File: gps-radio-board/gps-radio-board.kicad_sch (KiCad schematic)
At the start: 61 parts, among them J1 SMA, J2 SMA, J3 USB_C_Receptacle_USB2.0_16P, J4 JST_BATT, J5 Conn_01x04, J6 Conn_01x04, J7 Conn_01x04, J8 DM3CS-SF, U1 ESP32-C6-MINI-1U-H4, U3 SiP32431DR3, U4 AP2112K-3.3, U5 MAX-M10N, U6 MCP73831, U7 AP2112K-3.3

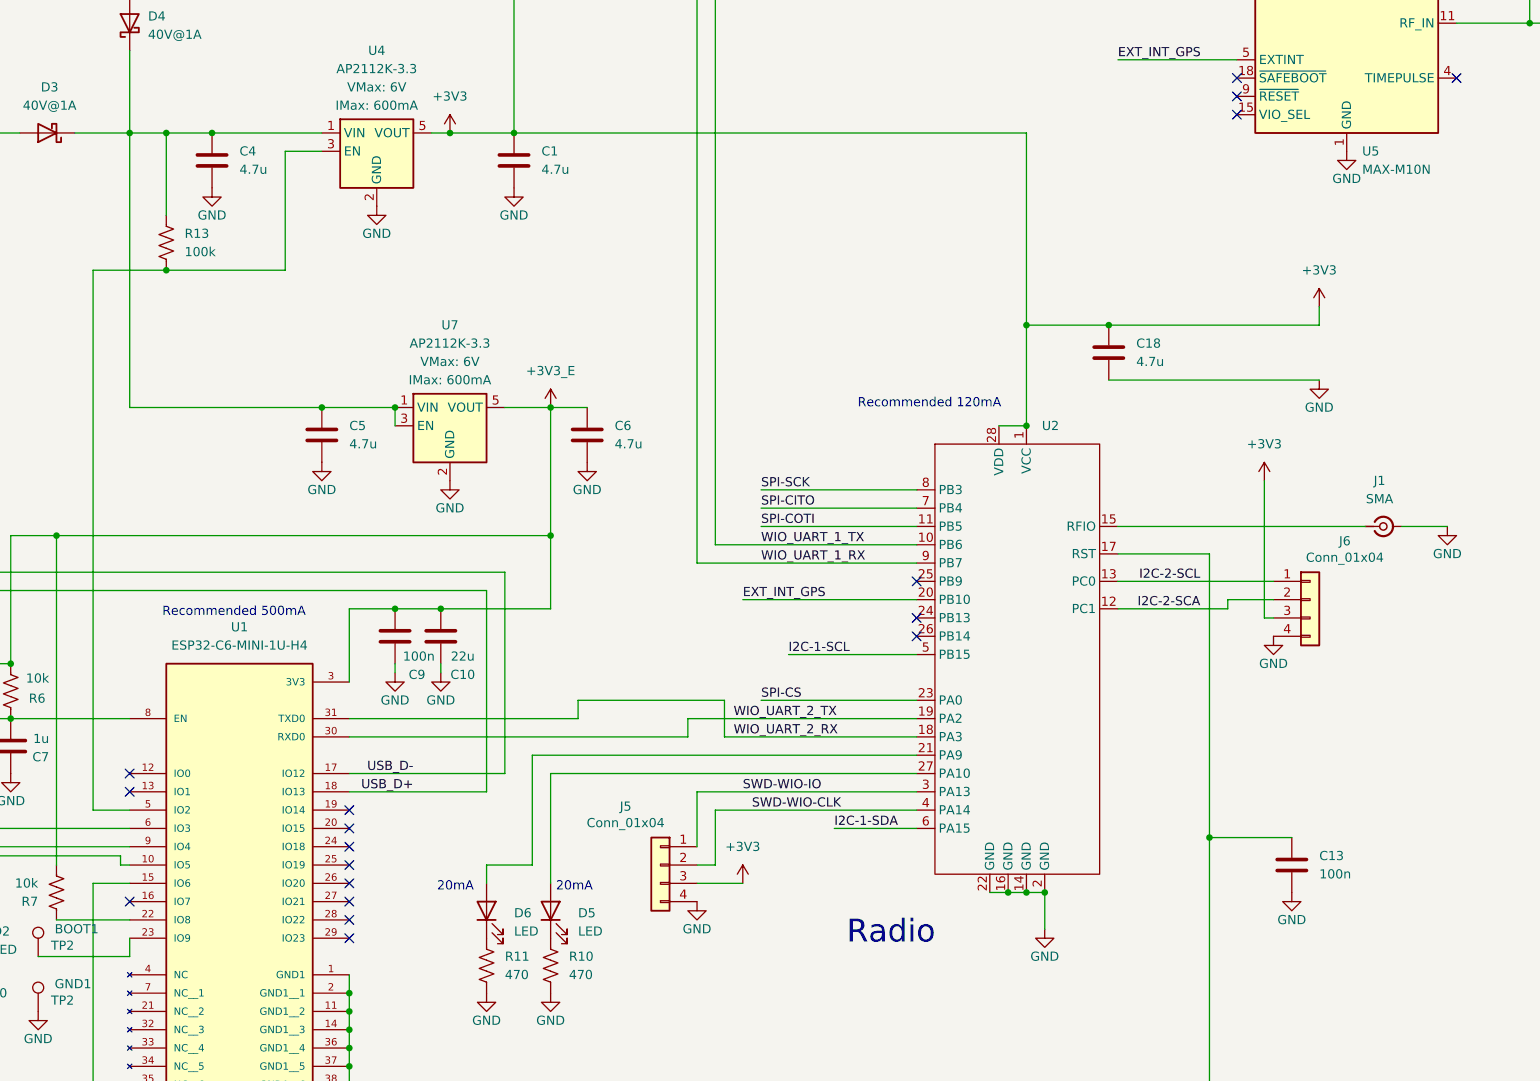
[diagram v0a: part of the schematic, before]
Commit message: Layout fixes. Swap 100k ref for en
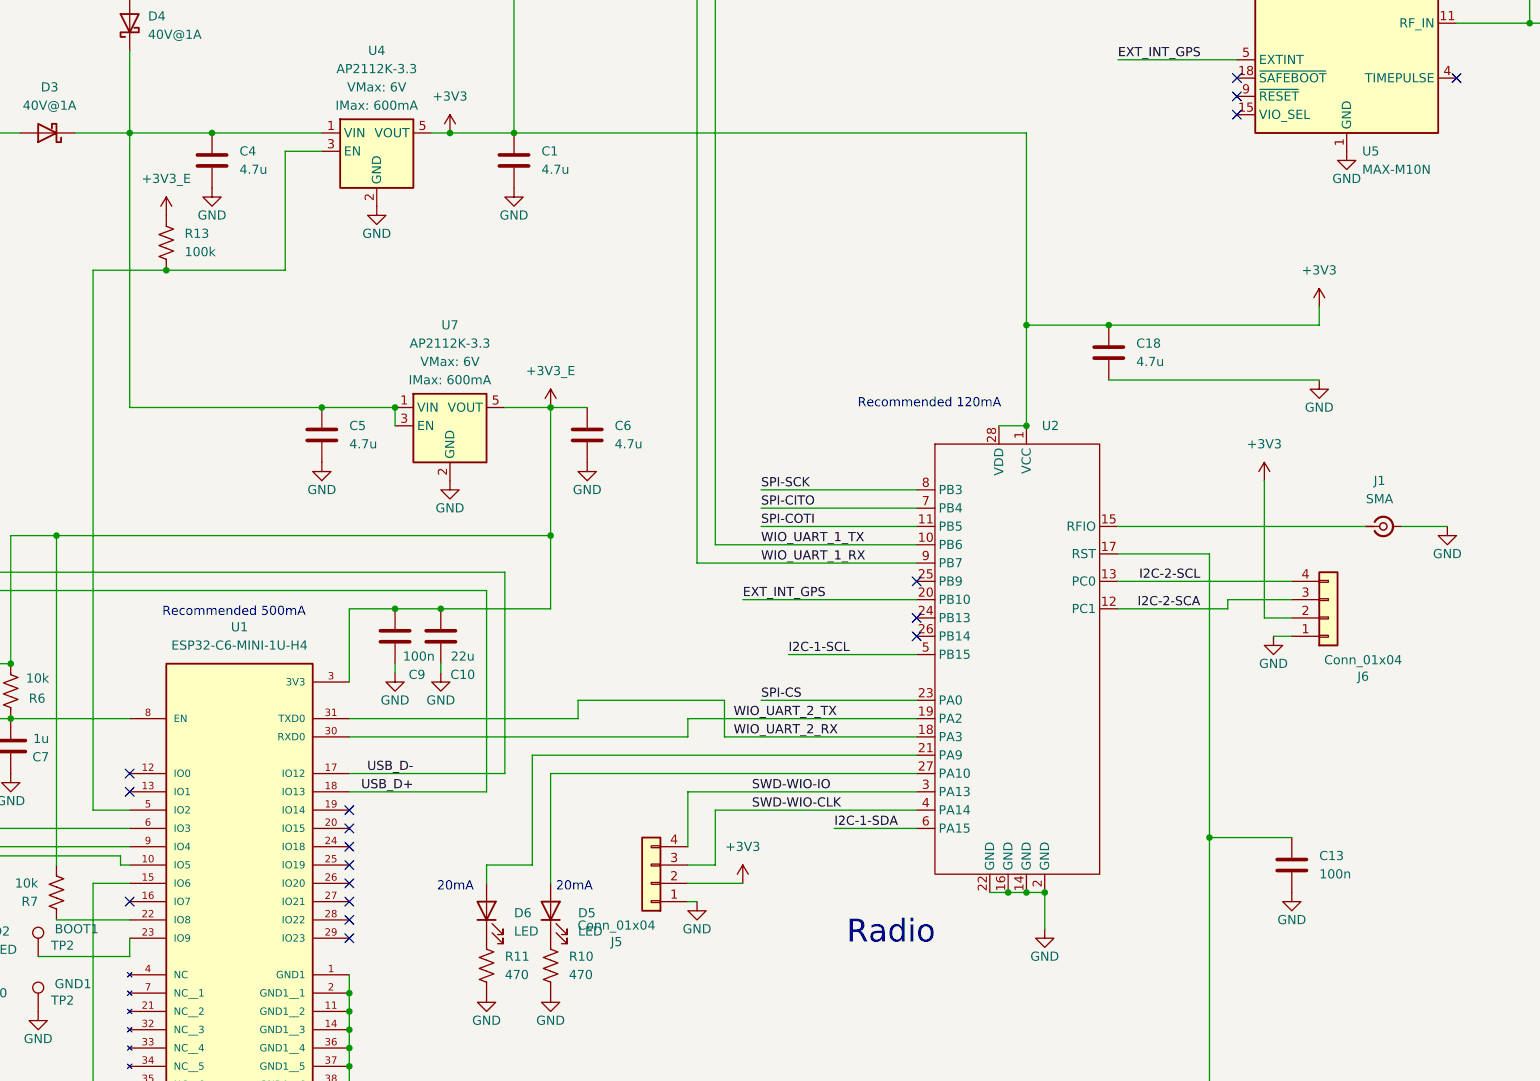
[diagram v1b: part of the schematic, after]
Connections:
- net +3V3: now also J5.2 (Pin_2), J6.2 (Pin_2); no longer J5.3 (Pin_3), J6.3 (Pin_3)
- net +3V3_E: now also R13.2
- net GND: now also J5.1 (Pin_1), J6.1 (Pin_1); no longer J5.4 (Pin_4), J6.4 (Pin_4)
- net I2C-2-SCA: now also J6.3 (Pin_3); no longer J6.2 (Pin_2)
- net I2C-2-SCL: now also J6.4 (Pin_4); no longer J6.1 (Pin_1)
- net SWD-WIO-CLK: now also J5.3 (Pin_3); no longer J5.2 (Pin_2)
- net SWD-WIO-IO: now also J5.4 (Pin_4); no longer J5.1 (Pin_1)
- net at C4.1, C5.1, D3.1 (K)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: no longer R13.2
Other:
- moved on the sheet: J5, J6
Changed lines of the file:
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@@
 	)
 	(junction
-		(at 224.79 132.08)
-		(diameter 0)
-		(color 0 0 0 0)
-	)
-	(junction
 		(at 250.19 287.02)
 		(diameter 0)
@@
 	(wire
 		(pts
+			(xy 356.87 194.31) (xy 381 194.31)
+		)
+		(stroke
+			(width 0)
+			(type default)
+		)
+	)
+	(wire
+		(pts
 			(xy 241.3 134.62) (xy 241.3 151.13)
 		)
@@
 	(wire
 		(pts
+			(xy 297.18 238.76) (xy 298.45 238.76)
+		)
+		(stroke
+			(width 0)
+			(type default)
+		)
+	)
+	(wire
+		(pts
 			(xy 189.23 232.41) (xy 189.23 237.49)
 		)
@@
 	(wire
 		(pts
-			(xy 298.45 233.68) (xy 300.99 233.68)
-		)
-		(stroke
-			(width 0)
-			(type default)
-		)
-	)
-	(wire
-		(pts
-			(xy 304.8 236.22) (xy 298.45 236.22)
-		)
-		(stroke
-			(width 0)
-			(type default)
-		)
-	)
-	(wire
-		(pts
 			(xy 383.54 99.06) (xy 386.08 99.06)
 		)
@@
 	(wire
 		(pts
-			(xy 224.79 132.08) (xy 224.79 143.51)
-		)
-		(stroke
-			(width 0)
-			(type default)
-		)
-	)
-	(wire
-		(pts
 			(xy 344.17 132.08) (xy 344.17 158.75)
 		)
@@
 	(wire
 		(pts
-			(xy 219.71 132.08) (xy 224.79 132.08)
-		)
-		(stroke
-			(width 0)
-			(type default)
-		)
-	)
-	(wire
-		(pts
 			(xy 344.17 158.75) (xy 344.17 172.72)
 		)
@@
 	(wire
 		(pts
-			(xy 377.19 199.39) (xy 378.46 199.39)
+			(xy 355.6 166.37) (xy 384.81 166.37)
 		)
 		(stroke
@@
 	(wire
 		(pts
-			(xy 355.6 166.37) (xy 384.81 166.37)
+			(xy 381 201.93) (xy 378.46 201.93)
 		)
 		(stroke
@@
 	(wire
 		(pts
+			(xy 377.19 199.39) (xy 381 199.39)
+		)
+		(stroke
+			(width 0)
+			(type default)
+		)
+	)
+	(wire
+		(pts
 			(xy 250.19 254) (xy 250.19 256.54)
 		)
@@
 	(wire
 		(pts
-			(xy 224.79 132.08) (xy 231.14 132.08)
+			(xy 219.71 132.08) (xy 231.14 132.08)
 		)
 		(stroke
@@
 	(wire
 		(pts
+			(xy 297.18 233.68) (xy 300.99 233.68)
+		)
+		(stroke
+			(width 0)
+			(type default)
+		)
+	)
+	(wire
+		(pts
 			(xy 194.31 163.83) (xy 186.69 163.83)
 		)
@@
 	(wire
 		(pts
-			(xy 372.11 196.85) (xy 378.46 196.85)
+			(xy 160.02 146.05) (xy 176.53 146.05)
 		)
 		(stroke
@@
 	(wire
 		(pts
-			(xy 160.02 146.05) (xy 176.53 146.05)
+			(xy 137.16 220.98) (xy 158.75 220.98)
 		)
 		(stroke
@@
 	(wire
 		(pts
-			(xy 137.16 220.98) (xy 158.75 220.98)
+			(xy 297.18 223.52) (xy 328.93 223.52)
 		)
 		(stroke
@@
 	(wire
 		(pts
-			(xy 298.45 223.52) (xy 328.93 223.52)
+			(xy 297.18 236.22) (xy 304.8 236.22)
 		)
 		(stroke
@@
 	(wire
 		(pts
-			(xy 298.45 231.14) (xy 298.45 223.52)
+			(xy 297.18 231.14) (xy 297.18 223.52)
 		)
 		(stroke
@@
 	(wire
 		(pts
+			(xy 372.11 196.85) (xy 381 196.85)
+		)
+		(stroke
+			(width 0)
+			(type default)
+		)
+	)
+	(wire
+		(pts
 			(xy 250.19 317.5) (xy 250.19 320.04)
 		)
@@
 	(wire
 		(pts
-			(xy 356.87 194.31) (xy 378.46 194.31)
-		)
-		(stroke
-			(width 0)
-			(type default)
-		)
-	)
-	(wire
-		(pts
 			(xy 250.19 312.42) (xy 250.19 314.96)
 		)
@@
 	)
 	(label "SWD-WIO-IO"
-		(at 304.8 223.52 0)
+		(at 306.07 223.52 0)
 		(effects
 			(font
@@
 	(symbol
 		(lib_id "Connector_Generic:Conn_01x04")
-		(at 293.37 233.68 0)
-		(mirror y)
+		(at 292.1 236.22 180)
 		(unit 1)
 		(body_style 1)
@@
 		(dnp no)
 		(property "Reference" "J5"
-			(at 288.544 225.552 0)
+			(at 287.274 244.348 0)
 			(show_name no)
 			(do_not_autoplace no)
@@
 		)
 		(property "Value" "Conn_01x04"
-			(at 288.544 227.838 0)
+			(at 287.274 242.062 0)
 			(show_name no)
 			(do_not_autoplace no)
@@
 		)
 		(property "Footprint" "Connector_JST:JST_SH_BM04B-SRSS-TB_1x04-1MP_P1.00mm_Vertical"
-			(at 293.37 233.68 0)
+			(at 292.1 236.22 0)
 			(hide yes)
 			(show_name no)
@@
 		)
 		(property "Datasheet" ""
-			(at 293.37 233.68 0)
+			(at 292.1 236.22 0)
 			(hide yes)
 			(show_name no)
@@
 		)
 		(property "Description" "Generic connector, single row, 01x04, script generated (kicad-library-utils/schlib/autogen/connector/)"
-			(at 293.37 233.68 0)
+			(at 292.1 236.22 0)
 			(hide yes)
 			(show_name no)
@@
 	)
 	(symbol
+		(lib_id "power:+3V3")
+		(at 224.79 143.51 0)
+		(unit 1)
+		(body_style 1)
+		(exclude_from_sim no)
+		(in_bom yes)
+		(on_board yes)
+		(in_pos_files yes)
+		(dnp no)
+		(fields_autoplaced yes)
+		(property "Reference" "#PWR051"
+			(at 224.79 147.32 0)
+			(hide yes)
+			(show_name no)
+			(do_not_autoplace no)
+			(effects
+				(font
+					(size 1.27 1.27)
+				)
+			)
+		)
+		(property "Value" "+3V3_E"
+			(at 224.79 138.43 0)
+			(show_name no)
+			(do_not_autoplace no)
+			(effects
+				(font
+					(size 1.27 1.27)
+				)
+			)
+		)
+		(property "Footprint" ""
+			(at 224.79 143.51 0)
+			(hide yes)
+			(show_name no)
+			(do_not_autoplace no)
+			(effects
+				(font
+					(size 1.27 1.27)
+				)
+			)
+		)
+		(property "Datasheet" ""
+			(at 224.79 143.51 0)
+			(hide yes)
+			(show_name no)
+			(do_not_autoplace no)
+			(effects
+				(font
+					(size 1.27 1.27)
+				)
+			)
+		)
+		(property "Description" "Power symbol creates a global label with name \"+3V3\""
+			(at 224.79 143.51 0)
+			(hide yes)
+			(show_name no)
+			(do_not_autoplace no)
+			(effects
+				(font
+					(size 1.27 1.27)
+				)
+			)
+		)
+		(pin "1"
+		)
+		(instances
+			(project "gps-radio-board"
+				(path "/6516832b-56dd-436b-980b-7ee5d107ab91"
+					(reference "#PWR051")
+					(unit 1)
+				)
+			)
+		)
+	)
+	(symbol
 		(lib_id "PCM_SparkFun-PowerSymbol:GND")
 		(at 180.34 134.62 0)
@@
 	(symbol
 		(lib_id "Connector_Generic:Conn_01x04")
-		(at 383.54 196.85 0)
+		(at 386.08 199.39 0)
+		(mirror x)
 		(unit 1)
 		(body_style 1)
@@
 		(dnp no)
 		(property "Reference" "J6"
-			(at 388.366 188.722 0)
+			(at 390.906 207.518 0)
 			(show_name no)
 			(do_not_autoplace no)
@@
 		)
 		(property "Value" "Conn_01x04"
-			(at 388.366 191.008 0)
+			(at 390.906 205.232 0)
 			(show_name no)
 			(do_not_autoplace no)
@@
 		)
 		(property "Footprint" "Connector_JST:JST_SH_BM04B-SRSS-TB_1x04-1MP_P1.00mm_Vertical"
-			(at 383.54 196.85 0)
+			(at 386.08 199.39 0)
 			(hide yes)
 			(show_name no)
@@
 		)
 		(property "Datasheet" ""
-			(at 383.54 196.85 0)
+			(at 386.08 199.39 0)
 			(hide yes)
 			(show_name no)
@@
 		)
 		(property "Description" "Generic connector, single row, 01x04, script generated (kicad-library-utils/schlib/autogen/connector/)"
-			(at 383.54 196.85 0)
+			(at 386.08 199.39 0)
 			(hide yes)
 			(show_name no)

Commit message: Add output cap for battery charger
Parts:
- added C20: 4.7u, Capacitor_SMD:C_0603_1608Metric_Pad1.08x0.95mm_HandSolder, symbol Device:C
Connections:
- net +BATT: now also C20.1
- net GND: now also C20.2
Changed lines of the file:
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@@
 	)
 	(junction
+		(at 194.31 163.83)
+		(diameter 0)
+		(color 0 0 0 0)
+	)
+	(junction
 		(at 447.04 118.11)
 		(diameter 0)
@@
 	(wire
 		(pts
+			(xy 196.85 163.83) (xy 194.31 163.83)
+		)
+		(stroke
+			(width 0)
+			(type default)
+		)
+	)
+	(wire
+		(pts
 			(xy 256.54 205.74) (xy 256.54 207.01)
 		)
@@
 	)
 	(symbol
+		(lib_id "Device:C")
+		(at 196.85 167.64 0)
+		(unit 1)
+		(body_style 1)
+		(exclude_from_sim no)
+		(in_bom yes)
+		(on_board yes)
+		(in_pos_files yes)
+		(dnp no)
+		(fields_autoplaced yes)
+		(property "Reference" "C20"
+			(at 200.66 166.3699 0)
+			(show_name no)
+			(do_not_autoplace no)
+			(effects
+				(font
+					(size 1.27 1.27)
+				)
+				(justify left)
+			)
+		)
+		(property "Value" "4.7u"
+			(at 200.66 168.9099 0)
+			(show_name no)
+			(do_not_autoplace no)
+			(effects
+				(font
+					(size 1.27 1.27)
+				)
+				(justify left)
+			)
+		)
+		(property "Footprint" "Capacitor_SMD:C_0603_1608Metric_Pad1.08x0.95mm_HandSolder"
+			(at 197.8152 171.45 0)
+			(hide yes)
+			(show_name no)
+			(do_not_autoplace no)
+			(effects
+				(font
+					(size 1.27 1.27)
+				)
+			)
+		)
+		(property "Datasheet" ""
+			(at 196.85 167.64 0)
+			(hide yes)
+			(show_name no)
+			(do_not_autoplace no)
+			(effects
+				(font
+					(size 1.27 1.27)
+				)
+			)
+		)
+		(property "Description" "Unpolarized capacitor"
+			(at 196.85 167.64 0)
+			(hide yes)
+			(show_name no)
+			(do_not_autoplace no)
+			(effects
+				(font
+					(size 1.27 1.27)
+				)
+			)
+		)
+		(pin "1"
+		)
+		(pin "2"
+		)
+		(instances
+			(project "gps-radio-board"
+				(path "/6516832b-56dd-436b-980b-7ee5d107ab91"
+					(reference "C20")
+					(unit 1)
+				)
+			)
+		)
+	)
+	(symbol
 		(lib_id "PCM_SparkFun-PowerSymbol:GND")
 		(at 378.46 201.93 0)
@@
 					(unit 1)
 				)
+			)
+		)
+	)
+	(symbol
+		(lib_id "PCM_SparkFun-PowerSymbol:GND")
+		(at 196.85 171.45 0)
+		(unit 1)
+		(body_style 1)
+		(exclude_from_sim no)
+		(in_bom yes)
+		(on_board yes)
+		(in_pos_files yes)
+		(dnp no)
+		(fields_autoplaced yes)
+		(property "Reference" "#PWR052"
+			(at 196.85 177.8 0)
+			(hide yes)
+			(show_name no)
+			(do_not_autoplace no)
+			(effects
+				(font
+					(size 1.27 1.27)
+				)
+			)
+		)
+		(property "Value" "GND"
+			(at 196.85 175.26 0)
+			(show_name no)
+			(do_not_autoplace yes)
+			(effects
+				(font
+					(size 1.27 1.27)
+				)
+			)
+		)
+		(property "Footprint" ""
+			(at 196.85 171.45 0)
+			(hide yes)
+			(show_name no)
+			(do_not_autoplace no)
+			(effects
+				(font
+					(size 1.27 1.27)
+				)
+			)
+		)
+		(property "Datasheet" ""
+			(at 196.85 171.45 0)
+			(hide yes)
+			(show_name no)
+			(do_not_autoplace no)
+			(effects
+				(font
+					(size 1.27 1.27)
+				)
+			)
+		)
+		(property "Description" "Power symbol creates a global label with name \"GND\" , ground"
+			(at 196.85 180.34 0)
+			(hide yes)
+			(show_name no)
+			(do_not_autoplace no)
+			(effects
+				(font
+					(size 1.27 1.27)
+				)
+			)
+		)
+		(pin "1"
+		)
+		(instances
+			(project "gps-radio-board"
+				(path "/6516832b-56dd-436b-980b-7ee5d107ab91"
+					(reference "#PWR052")
+					(unit 1)
+				)

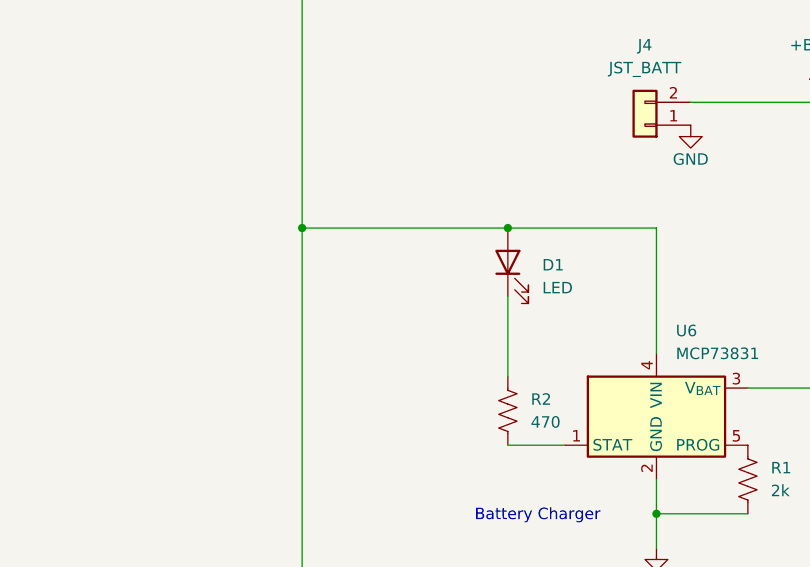
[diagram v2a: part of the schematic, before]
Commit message: Add input cap for battery
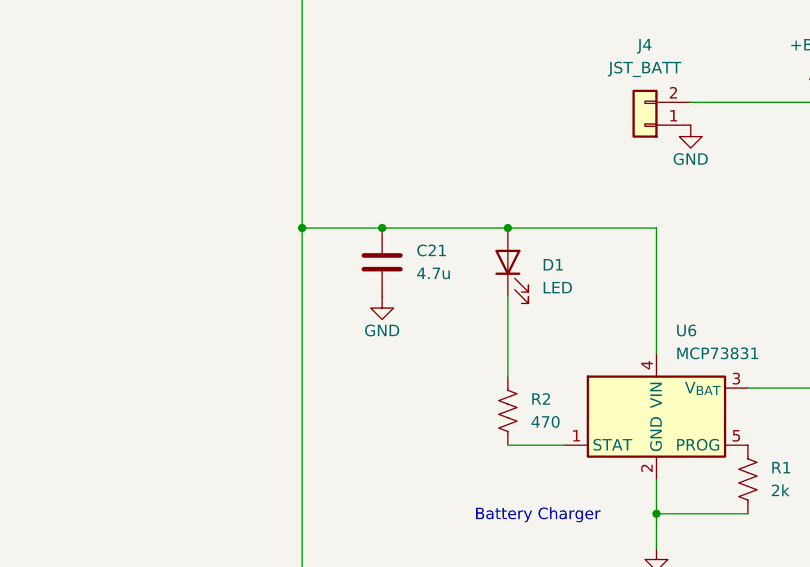
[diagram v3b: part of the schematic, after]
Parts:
- added C21: 4.7u, Capacitor_SMD:C_0603_1608Metric_Pad1.08x0.95mm_HandSolder, symbol Device:C
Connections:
- net GND: now also C21.2
- net USB_IN: now also C21.1
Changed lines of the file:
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@@
 	)
 	(junction
+		(at 146.05 146.05)
+		(diameter 0)
+		(color 0 0 0 0)
+	)
+	(junction
 		(at 250.19 304.8)
 		(diameter 0)
@@
 	(wire
 		(pts
-			(xy 137.16 146.05) (xy 160.02 146.05)
+			(xy 137.16 146.05) (xy 146.05 146.05)
 		)
 		(stroke
@@
 	(wire
 		(pts
+			(xy 146.05 146.05) (xy 160.02 146.05)
+		)
+		(stroke
+			(width 0)
+			(type default)
+		)
+	)
+	(wire
+		(pts
 			(xy 250.19 281.94) (xy 250.19 284.48)
 		)
@@
 	(symbol
 		(lib_id "Device:C")
+		(at 146.05 149.86 0)
+		(unit 1)
+		(body_style 1)
+		(exclude_from_sim no)
+		(in_bom yes)
+		(on_board yes)
+		(in_pos_files yes)
+		(dnp no)
+		(fields_autoplaced yes)
+		(property "Reference" "C21"
+			(at 149.86 148.5899 0)
+			(show_name no)
+			(do_not_autoplace no)
+			(effects
+				(font
+					(size 1.27 1.27)
+				)
+				(justify left)
+			)
+		)
+		(property "Value" "4.7u"
+			(at 149.86 151.1299 0)
+			(show_name no)
+			(do_not_autoplace no)
+			(effects
+				(font
+					(size 1.27 1.27)
+				)
+				(justify left)
+			)
+		)
+		(property "Footprint" "Capacitor_SMD:C_0603_1608Metric_Pad1.08x0.95mm_HandSolder"
+			(at 147.0152 153.67 0)
+			(hide yes)
+			(show_name no)
+			(do_not_autoplace no)
+			(effects
+				(font
+					(size 1.27 1.27)
+				)
+			)
+		)
+		(property "Datasheet" ""
+			(at 146.05 149.86 0)
+			(hide yes)
+			(show_name no)
+			(do_not_autoplace no)
+			(effects
+				(font
+					(size 1.27 1.27)
+				)
+			)
+		)
+		(property "Description" "Unpolarized capacitor"
+			(at 146.05 149.86 0)
+			(hide yes)
+			(show_name no)
+			(do_not_autoplace no)
+			(effects
+				(font
+					(size 1.27 1.27)
+				)
+			)
+		)
+		(pin "1"
+		)
+		(pin "2"
+		)
+		(instances
+			(project "gps-radio-board"
+				(path "/6516832b-56dd-436b-980b-7ee5d107ab91"
+					(reference "C21")
+					(unit 1)
+				)
+			)
+		)
+	)
+	(symbol
+		(lib_id "Device:C")
 		(at 196.85 167.64 0)
 		(unit 1)
@@
 					(unit 1)
 				)
+			)
+		)
+	)
+	(symbol
+		(lib_id "PCM_SparkFun-PowerSymbol:GND")
+		(at 146.05 153.67 0)
+		(unit 1)
+		(body_style 1)
+		(exclude_from_sim no)
+		(in_bom yes)
+		(on_board yes)
+		(in_pos_files yes)
+		(dnp no)
+		(fields_autoplaced yes)
+		(property "Reference" "#PWR053"
+			(at 146.05 160.02 0)
+			(hide yes)
+			(show_name no)
+			(do_not_autoplace no)
+			(effects
+				(font
+					(size 1.27 1.27)
+				)
+			)
+		)
+		(property "Value" "GND"
+			(at 146.05 157.48 0)
+			(show_name no)
+			(do_not_autoplace yes)
+			(effects
+				(font
+					(size 1.27 1.27)
+				)
+			)
+		)
+		(property "Footprint" ""
+			(at 146.05 153.67 0)
+			(hide yes)
+			(show_name no)
+			(do_not_autoplace no)
+			(effects
+				(font
+					(size 1.27 1.27)
+				)
+			)
+		)
+		(property "Datasheet" ""
+			(at 146.05 153.67 0)
+			(hide yes)
+			(show_name no)
+			(do_not_autoplace no)
+			(effects
+				(font
+					(size 1.27 1.27)
+				)
+			)
+		)
+		(property "Description" "Power symbol creates a global label with name \"GND\" , ground"
+			(at 146.05 162.56 0)
+			(hide yes)
+			(show_name no)
+			(do_not_autoplace no)
+			(effects
+				(font
+					(size 1.27 1.27)
+				)
+			)
+		)
+		(pin "1"
+		)
+		(instances
+			(project "gps-radio-board"
+				(path "/6516832b-56dd-436b-980b-7ee5d107ab91"
+					(reference "#PWR053")
+					(unit 1)
+				)
